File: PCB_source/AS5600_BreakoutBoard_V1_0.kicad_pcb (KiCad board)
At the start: 2 copper layers, 20 x 13.5 mm, 22 parts, among them P1 CONN_01X06, P2 MountHole_M3, P3 MountHole_M3, U1 AS5600

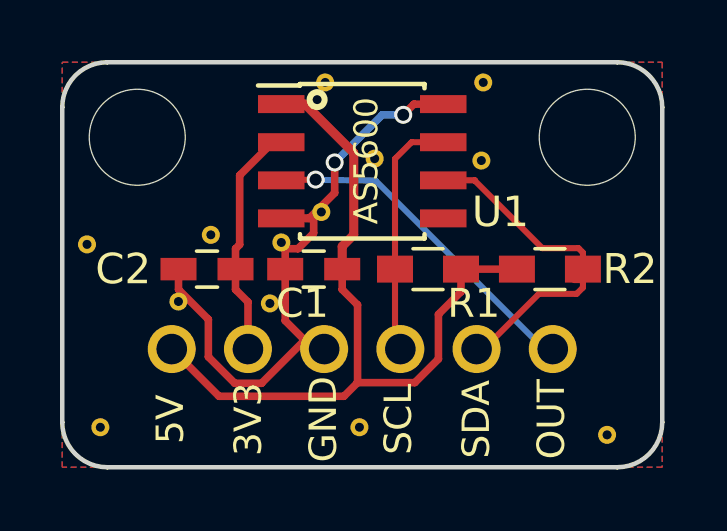
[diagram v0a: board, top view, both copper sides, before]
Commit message: add step and refactoring
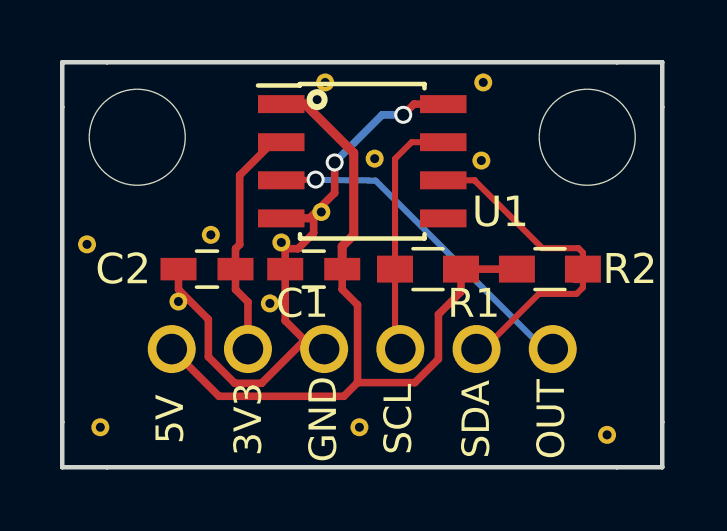
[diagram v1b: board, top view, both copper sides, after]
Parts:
- C1, C2: footprint Capacitors_SMD:C_0603_HandSoldering -> footprints:C_0603_HandSoldering
- P1: footprint user:USER_SIL-6 -> footprints:USER_SIL-6
- R1, R2: footprint Resistors_SMD:R_0603_HandSoldering -> footprints:R_0603_HandSoldering
- U1: footprint Housings_SOIC:SOIC-8_3.9x4.9mm_Pitch1.27mm -> footprints:SOIC-8_3.9x4.9mm_Pitch1.27mm
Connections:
- P2 pad 1: (no net) -> Net-(P2-Pad1)
- P3 pad 1: (no net) -> Net-(P3-Pad1)
- U1 pad 5: (no net) -> Net-(U1-Pad5)
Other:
- outline, holes or cut-outs redrawn
- rule pad_to_mask_clearance: 0.2 -> 0
